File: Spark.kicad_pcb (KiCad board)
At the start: 2 copper layers, 36 x 36 mm, 87 parts, among them J0 Battery Pads, J1 SWD-PROG-6, SW1 UP, SW2 OK, SW3 DOWN, U0 ATSAMD21G18A-AUT, U1 BMA250E, U2 Reg, U3 CHG CTRL, Y1 32.768KHz

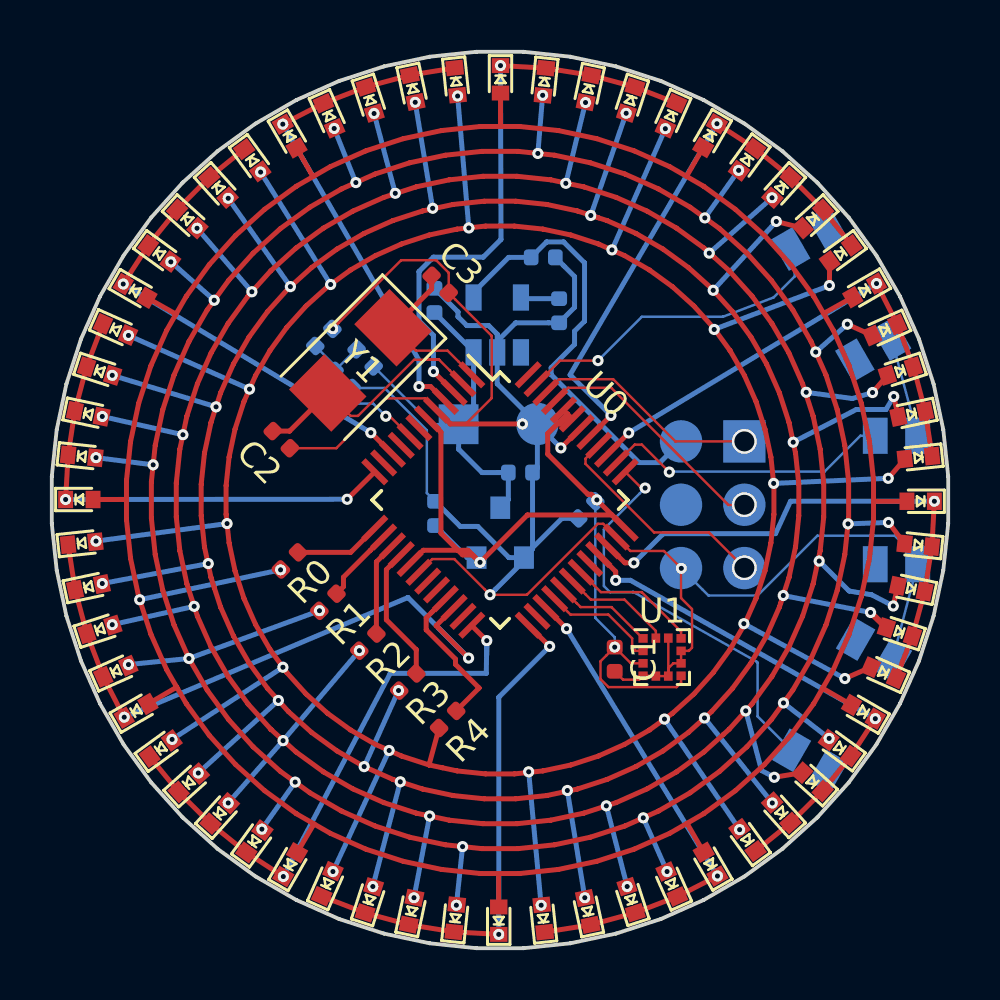
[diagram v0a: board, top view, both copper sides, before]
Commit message: initial rework to atmega1284p
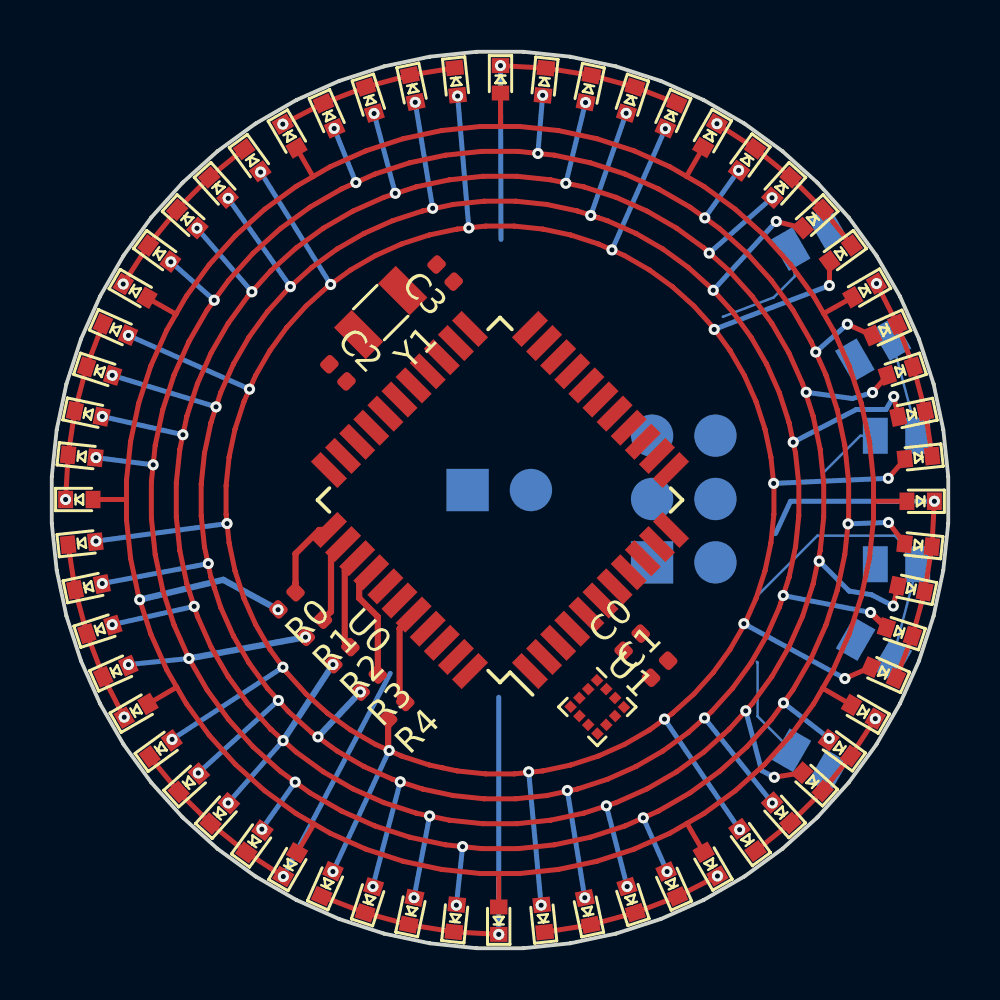
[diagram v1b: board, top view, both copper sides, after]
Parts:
- removed C4, C5, C6: 1uF, Capacitor_SMD:C_0402_1005Metric
- removed C7, C8: 4.7uF, Capacitor_SMD:C_0402_1005Metric
- removed R5, R6: 10M, Resistor_SMD:R_0402_1005Metric
- removed R7: 2K, Resistor_SMD:R_0402_1005Metric
- removed U2: Reg, Package_TO_SOT_SMD:SOT-23
- removed U3: CHG CTRL, Package_TO_SOT_SMD:SOT-23-5
- C0: moved to F.Cu
- J0: footprint Custom Footprints:150mAh-Lipo -> Custom_Footprints:2-pin-SMD
- J1: value SWD-PROG-6 -> ISP-PROG-6; footprint Custom Footprints:ISP_SMD -> Custom_Footprints:ISP_SMD
- U0: value ATSAMD21G18A-AUT -> ATmega1284P-AU; footprint Package_QFP:TQFP-48_7x7mm_P0.5mm -> Package_QFP:TQFP-44_10x10mm_P0.8mm
- U1: value BMA250E -> BMA280
- Y1: footprint Crystal:Crystal_SMD_5032-2Pin_5.0x3.2mm -> Crystal:Crystal_SMD_3215-2Pin_3.2x1.5mm
- moved J1 6.10 mm to (156.1, 52.5), turned to 0 degrees
- moved C0 5.61 mm to (155.3, 55.7), turned to 225 degrees
- moved J0 4.50 mm to (148.7, 49.6), turned to 270 degrees
- moved C2 3.51 mm to (143.5, 44.9), turned to 135 degrees
- moved U1 3.28 mm to (153.9, 58.3), turned to 315 degrees
- moved Y1 2.08 mm to (145.2, 42.5)
- moved R4 2.07 mm to (145.9, 58.4)
- moved C1 1.84 mm to (156.4, 56.8), turned to 45 degrees
- moved R0 1.60 mm to (141.5, 54.0)
- moved R3 1.54 mm to (144.8, 57.3)
- moved R1 1.18 mm to (142.6, 55.1)
- moved R2 1.18 mm to (143.7, 56.2)
- moved C3 0.49 mm to (147.8, 40.9), turned to 135 degrees
- turned U0 to 135 degrees
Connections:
- C0 pad 2: +3V3 -> +BATT
- C1 pad 1: +3V3 -> +BATT
- C2 pad 1: XOUT -> TOSC1
- C3 pad 1: XIN -> TOSC2
- J1 pad 1: SWDIO -> MISO
- J1 pad 2: CHARGE -> +BATT
- J1 pad 3: SWCLK -> SCK
- J1 pad 4: (no net) -> MOSI
- U0 pad 1: XIN -> MOSI
- U0 pad 10: TEN -> TWO
- U0 pad 11: (no net) -> THREE
- U0 pad 12: NINE -> FOUR
- U0 pad 13: Net-(R0-Pad1) -> FIVE
- U0 pad 14: Net-(R1-Pad1) -> SIX
- U0 pad 15: Net-(R2-Pad1) -> SEVEN
- U0 pad 16: Net-(R3-Pad1) -> EIGHT
- U0 pad 17: +3V3 -> +BATT
- U0 pad 19: (no net) -> NINE
- U0 pad 2: XOUT -> MISO
- U0 pad 20: (no net) -> TEN
- U0 pad 21: Net-(R4-Pad1) -> ELEVEN
- U0 pad 22: EIGHT -> TWELVE
- U0 pad 23: (no net) -> Net-(U0-Pad23)
- U0 pad 24: SEVEN -> Net-(U0-Pad24)
- U0 pad 25: SIX -> TOSC1
- U0 pad 26: (no net) -> TOSC2
- U0 pad 27: FIVE -> +BATT
- U0 pad 28: SDx -> GND
- U0 pad 29: SDO -> +BATT
- U0 pad 3: TWELVE -> SCK
- U0 pad 30: SCx -> BAT_MON
- U0 pad 31: CSB -> ACC_INT
- U0 pad 32: (no net) -> Net-(U0-Pad32)
- U0 pad 33: FOUR -> Net-(U0-Pad33)
- U0 pad 34: THREE -> Net-(R0-Pad1)
- U0 pad 35: GND -> Net-(R1-Pad1)
- U0 pad 36: +3V3 -> Net-(R2-Pad1)
- U0 pad 37: Net-(SW3-Pad2) -> Net-(R3-Pad1)
- U0 pad 38: Net-(SW2-Pad2) -> +BATT
- U0 pad 39: TWO -> GND
- U0 pad 4: ELEVEN -> RESET
- U0 pad 40: RESET -> Net-(R4-Pad1)
- U0 pad 41: ONE -> Net-(SW1-Pad2)
- U0 pad 42: GND -> Net-(SW3-Pad2)
- U0 pad 43: +3V3 -> Net-(SW2-Pad2)
- U0 pad 44: +3V3 -> CS
- U0 pad 5: GND -> +BATT
- U0 pad 6: +3V3 -> GND
- U0 pad 7: (no net) -> Net-(U0-Pad7)
- U0 pad 8: BAT_MON -> Net-(U0-Pad8)
- U0 pad 9: (no net) -> ONE
- U1 pad 1: SDO -> MISO
- U1 pad 10: CSB -> CS
- U1 pad 12: SCx -> SCK
- U1 pad 2: SDx -> MOSI
- U1 pad 3: +3V3 -> +BATT
- U1 pad 5: GND -> ACC_INT
- U1 pad 6: GND -> Net-(U1-Pad6)
- U1 pad 7: +3V3 -> +BATT
- Y1 pad 1: XIN -> TOSC2
- Y1 pad 2: XOUT -> TOSC1
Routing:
- net GND: track 105.4 -> 16.0 mm, vias 5 -> 0
- net +3V3: track 38.5 -> 0.00 mm, vias 3 -> 0
- net EIGHT: track 26.0 -> 7.35 mm, vias 2 -> 1
- net CHARGE: track 17.9 -> 0.00 mm
- net ONE: track 22.5 -> 7.34 mm, vias 2 -> 1
- net +BATT: track 14.8 -> 0.00 mm
- net ELEVEN: track 20.6 -> 7.30 mm, vias 2 -> 1
- net FOUR: track 20.4 -> 7.21 mm, vias 2 -> 1
- net NINE: track 20.1 -> 7.25 mm, vias 2 -> 1
- net TWO: track 20.1 -> 7.32 mm, vias 2 -> 1
- net FIVE: track 20.1 -> 7.34 mm, vias 2 -> 1
- net TEN: track 20.1 -> 7.32 mm, vias 2 -> 1
- net Net-(SW3-Pad2): track 16.8 -> 4.13 mm, vias 1 -> 0
- net XOUT: track 10.5 -> 0.00 mm
- net SWCLK: track 9.78 -> 0.00 mm, vias 1 -> 0
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
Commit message: erm, well, I did this ages ago so...
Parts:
- J0: footprint Custom_Footprints:2-pin-SMD -> Battery:BatteryHolder_Keystone_3002_1x2032
- moved J1 21.5 mm to (134.6, 52.5)
- moved C3 5.88 mm to (143.4, 44.8)
- moved C2 5.80 mm to (147.7, 40.9)
- moved J0 0.50 mm to (149.0, 50.0)
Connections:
- U0 pad 10: TWO -> Net-(U0-Pad10)
- U0 pad 11: THREE -> FIVE
- U0 pad 13: FIVE -> Net-(SW2-Pad2)
- U0 pad 14: SIX -> THREE
- U0 pad 15: SEVEN -> Net-(SW3-Pad2)
- U0 pad 16: EIGHT -> Net-(SW1-Pad2)
- U0 pad 19: NINE -> TWO
- U0 pad 20: TEN -> ONE
- U0 pad 21: ELEVEN -> TWELVE
- U0 pad 22: TWELVE -> ELEVEN
- U0 pad 32: Net-(U0-Pad32) -> TEN
- U0 pad 33: Net-(U0-Pad33) -> NINE
- U0 pad 41: Net-(SW1-Pad2) -> EIGHT
- U0 pad 42: Net-(SW3-Pad2) -> SEVEN
- U0 pad 43: Net-(SW2-Pad2) -> SIX
- U0 pad 9: ONE -> Net-(U0-Pad9)
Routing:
- net EIGHT: track 7.35 -> 24.4 mm, vias 1 -> 2
- net FOUR: track 7.21 -> 24.2 mm, vias 1 -> 2
- net GND: track 16.0 -> 0.00 mm
- net ELEVEN: track 7.30 -> 22.6 mm, vias 1 -> 2
- net TWO: track 7.32 -> 21.0 mm, vias 1 -> 2
- net ONE: track 7.34 -> 19.3 mm, vias 1 -> 2
- net Net-(SW3-Pad2): track 4.13 -> 14.8 mm, vias 0 -> 2
- net THREE: track 14.5 -> 22.1 mm, vias 1 -> 2
- net Net-(SW2-Pad2): track 2.63 -> 9.94 mm, vias 0 -> 2
- net M1: track 121.6 -> 128.3 mm, vias 25 -> 24
- net TWELVE: track 14.2 -> 20.2 mm, vias 1 -> 2
- net Net-(SW1-Pad2): track 4.50 -> 10.2 mm, vias 0 -> 2
- net TOSC2: track 0.00 -> 5.40 mm
- net TOSC1: track 0.00 -> 5.39 mm
- net M3: track 131.7 -> 136.8 mm, vias 26 -> 25
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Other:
- copper layers 2 -> 4
